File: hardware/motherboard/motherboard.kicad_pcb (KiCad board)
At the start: 4 copper layers, 152 x 68 mm, 79 parts, among them J1 IMU Connector, J2 JST-VH, J3 JST-VH, J4 JST-PH, J5 USB C 2.0, Q1 TSM7P06CP_ROG, Q2 TSM7P06CP_ROG, SW1 A, SW10 Right, SW11 Left, SW12 Up, SW2 B, SW3 X, SW4 Y, SW7 Start, SW8 Select, SW9 Down, U1 ESP32-S3-WROOM-1, U2 MCP73831-2-OT, U3 TPS75533KTTRG3, U4 TLV75709PDBV, U5 COM-09032

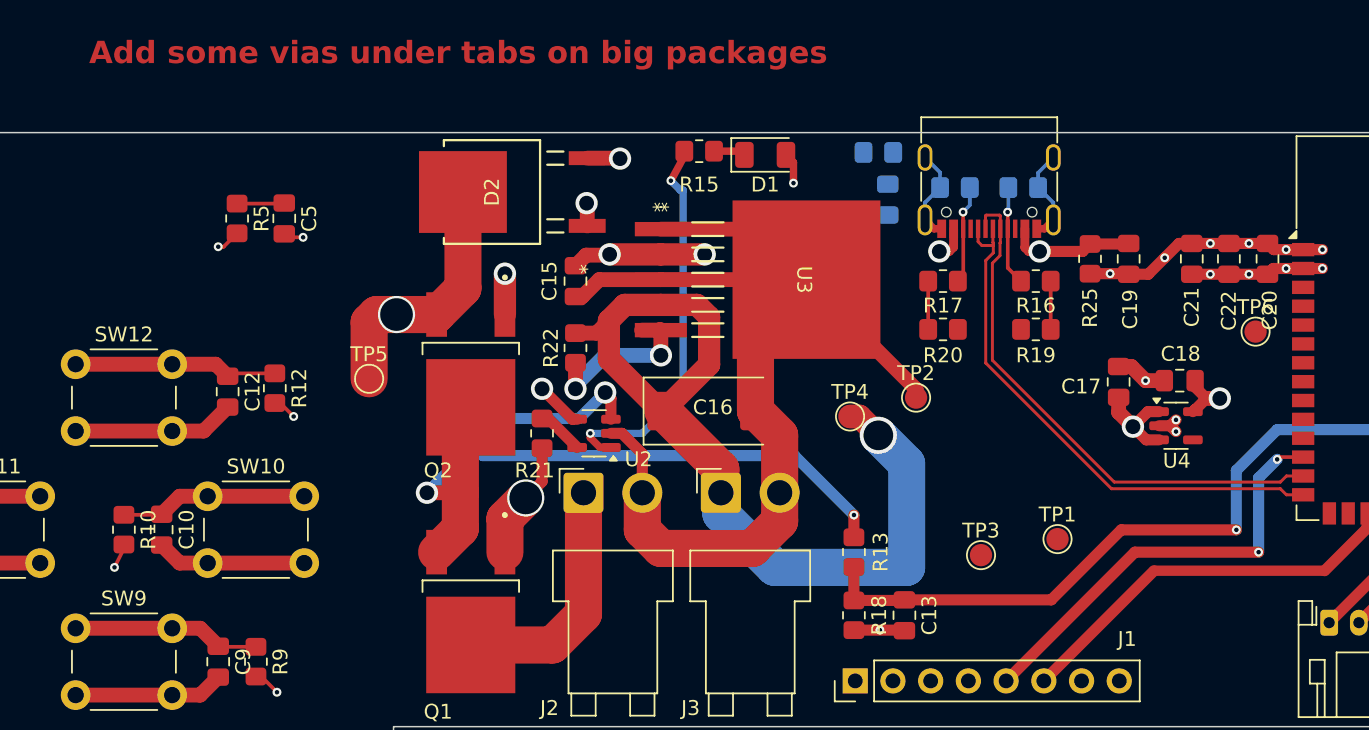
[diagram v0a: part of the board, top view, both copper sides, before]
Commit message: Moved Test Points
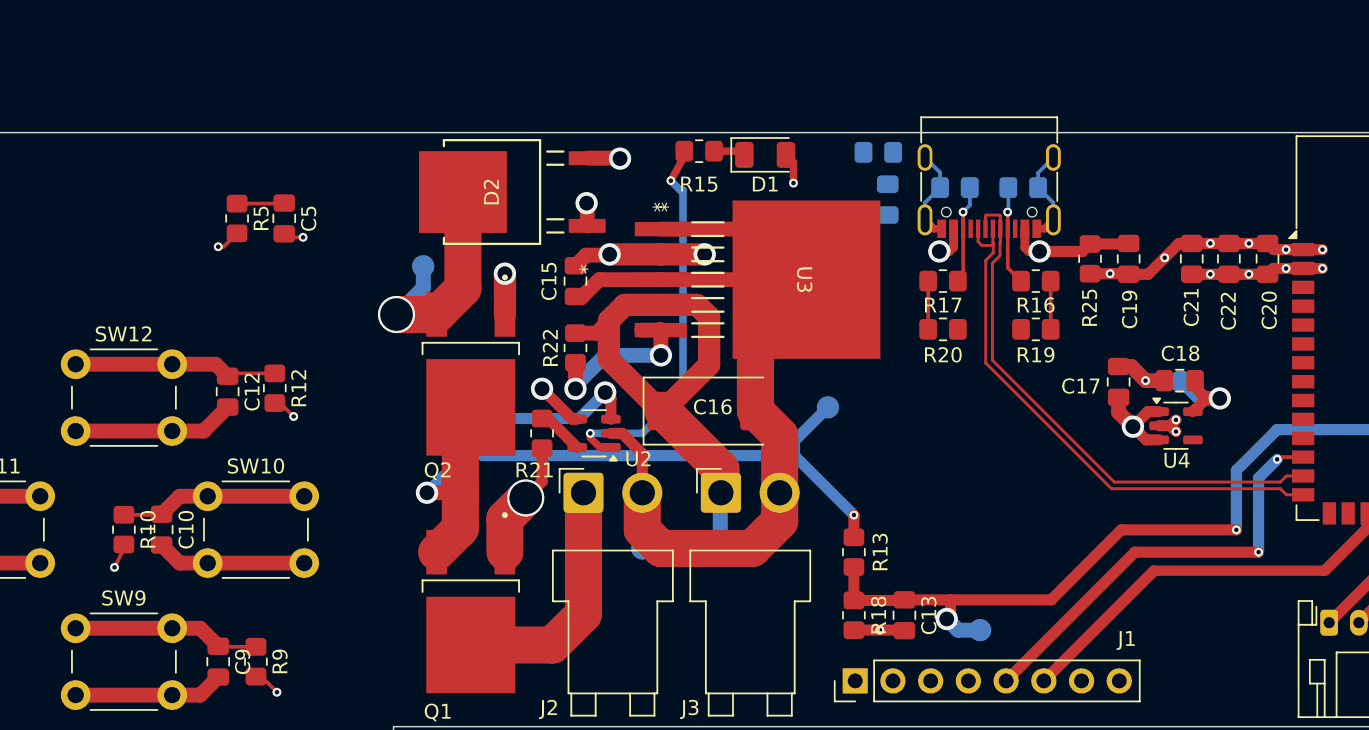
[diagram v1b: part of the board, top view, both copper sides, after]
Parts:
- TP1, TP2, TP3, TP4, TP5, TP6: moved to B.Cu
- moved TP2 21.0 mm to (64.8, 40.0), turned to 180 degrees
- moved TP3 14.3 mm to (77.2, 30.5), turned to 180 degrees
- moved TP4 12.5 mm to (70.0, 40.0), turned to 180 degrees
- moved TP5 8.41 mm to (50.0, 21.0), turned to 180 degrees
- moved TP1 8.04 mm to (87.5, 45.5), turned to 180 degrees
- moved TP6 6.06 mm to (101.0, 28.8), turned to 180 degrees
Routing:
- net VPeripheral: track 60.7 -> 36.3 mm, vias 1 -> 0
- net GND: track 234.5 -> 227.2 mm
- net VBat: track 73.5 -> 77.7 mm
- net ABat: track 65.4 -> 69.4 mm, vias 2 -> 3
- net +3V3: track 33.0 -> 36.1 mm
- net VIN: track 117.6 -> 115.7 mm
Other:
- board text removed: "Add some vias under tabs on big packages"

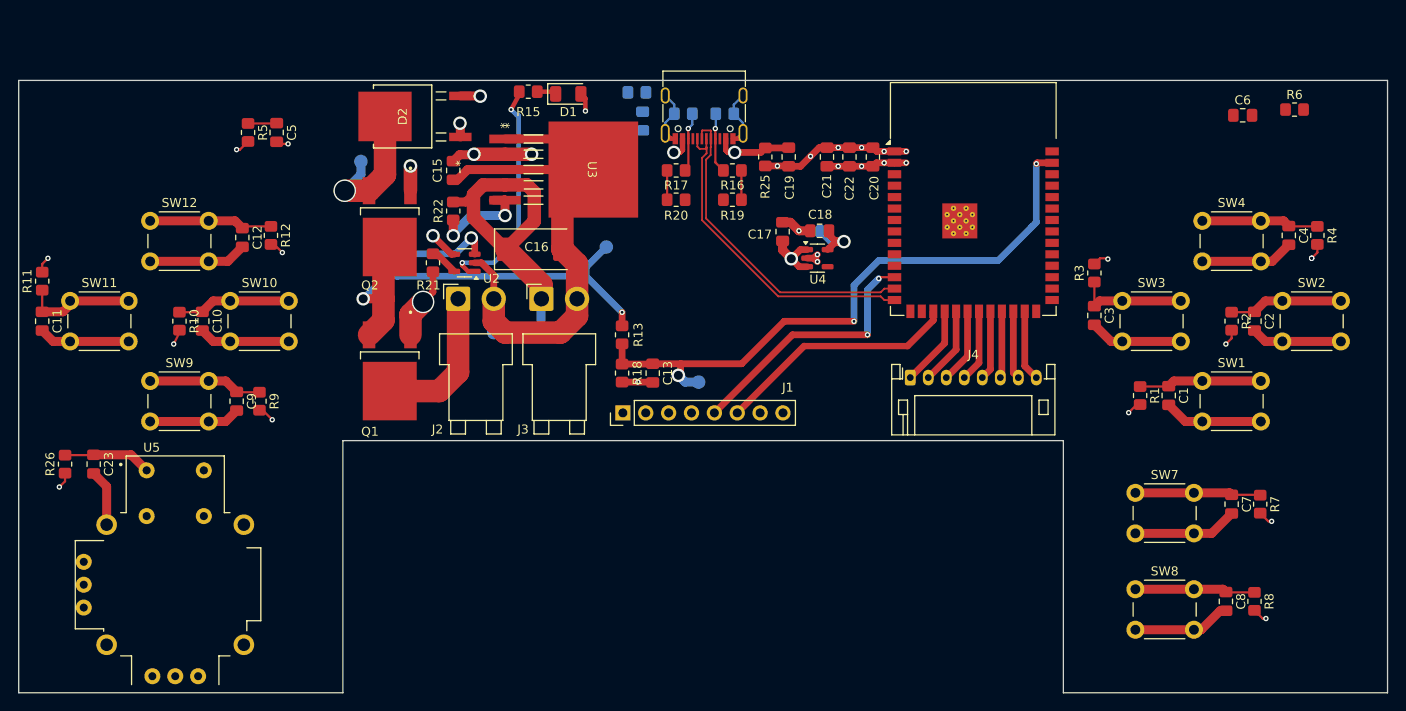
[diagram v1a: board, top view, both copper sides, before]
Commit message: Added bumper buttons
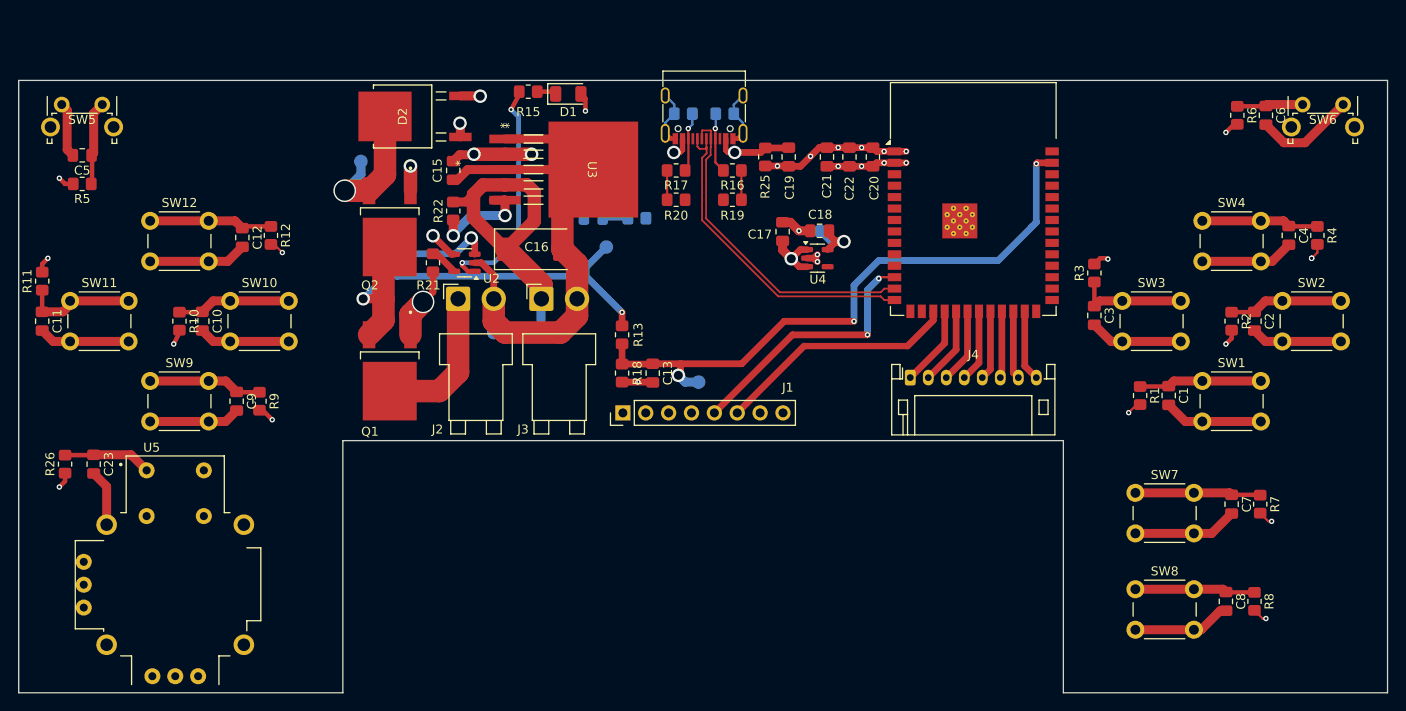
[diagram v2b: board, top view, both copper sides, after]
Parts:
- added SW5: LB, Button_Switch_THT:SW_Tactile_SPST_Angled_PTS645Vx58-2LFS, F.Cu at (16.8, 14.7)
- added SW6: RB, Button_Switch_THT:SW_Tactile_SPST_Angled_PTS645Vx58-2LFS, F.Cu at (154.6, 14.7)
- R21: value ??? -> 2k
- moved C5 21.7 mm to (19.1, 20.3), turned to 180 degrees
- moved R5 19.3 mm to (19.1, 23.5), turned to 180 degrees
- moved R14 14.0 mm to (80.6, 27.3), turned to 0 degrees
- moved C14 12.1 mm to (75.8, 27.3), turned to 180 degrees
- moved R6 6.38 mm to (147.3, 15.9), turned to -90 degrees
- moved C6 2.58 mm to (150.5, 15.9), turned to -90 degrees
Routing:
- net GND: track 227.2 -> 243.5 mm, vias 12 -> 11
- net BRight: track 0.00 -> 7.33 mm
- net BLeft: track 3.19 -> 9.37 mm
- net En: track 0.00 -> 2.81 mm
- net +3V3: track 36.1 -> 37.9 mm, vias 18 -> 19

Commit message: Adjusted Bumper Button Positions
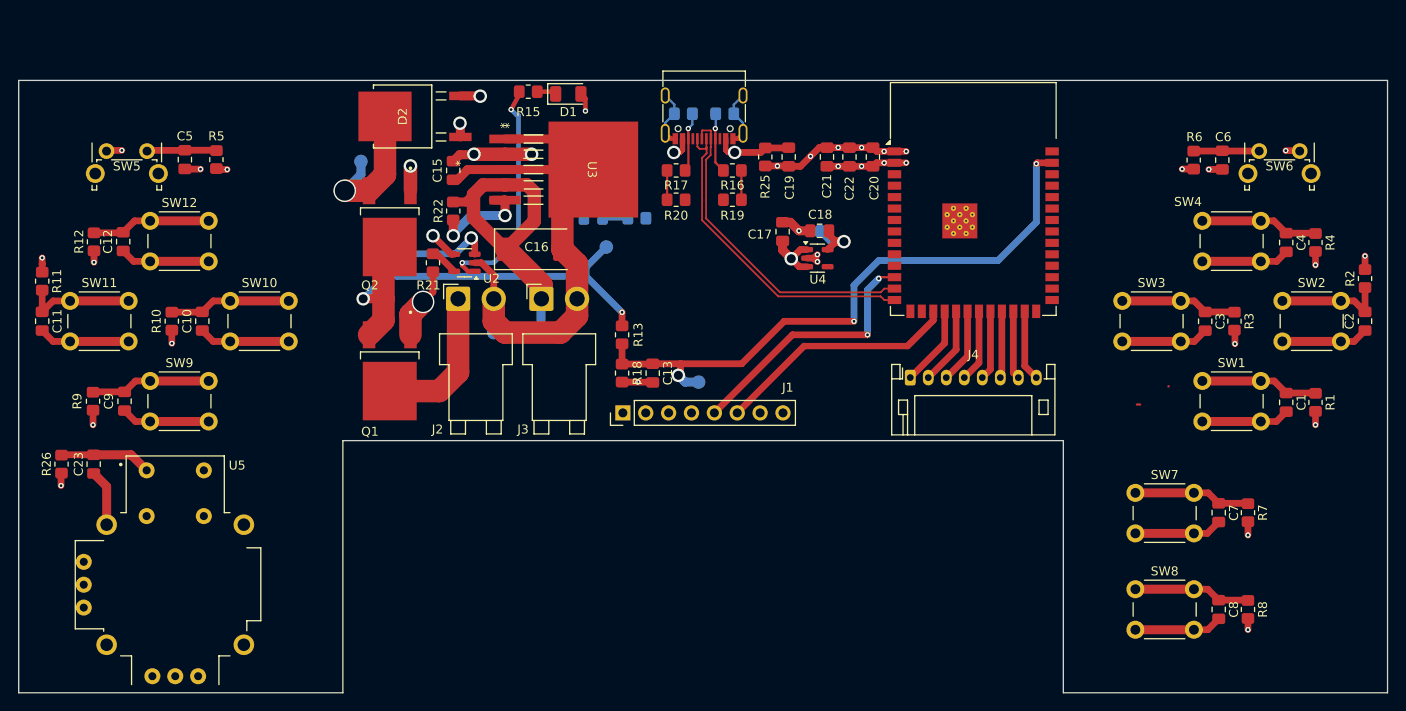
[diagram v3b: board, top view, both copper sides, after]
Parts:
- moved R12 19.7 mm to (20.4, 29.9)
- moved R1 19.5 mm to (156.0, 47.8)
- moved R9 18.5 mm to (20.2, 47.6)
- moved R3 16.4 mm to (147.0, 38.7), turned to -90 degrees
- moved R2 15.6 mm to (161.5, 34.0), turned to 90 degrees
- moved R5 15.1 mm to (34.0, 20.8), turned to -90 degrees
- moved C12 13.2 mm to (23.6, 29.9)
- moved C1 13.1 mm to (152.8, 47.8)
- moved C9 12.4 mm to (23.8, 47.6)
- moved C3 12.3 mm to (143.8, 38.8)
- moved C2 12.3 mm to (161.5, 38.7)
- moved C5 11.4 mm to (30.4, 20.8), turned to -90 degrees
- moved SW5 7.17 mm to (21.8, 19.9)
- moved SW6 7.07 mm to (149.8, 19.9)
- moved C6 6.94 mm to (145.7, 20.8)
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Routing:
- net GND: track 243.5 -> 224.8 mm, vias 11 -> 15
- net +3V3: track 37.9 -> 34.8 mm, vias 19 -> 18
- net BLeft: track 9.37 -> 7.76 mm
- net Start: track 14.0 -> 13.0 mm
- net Right: track 12.7 -> 13.5 mm
- net Down: track 12.7 -> 13.4 mm
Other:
- board text removed: "Left Bumper"
- board text removed: "Right Bumper"

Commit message: 12mm Corners
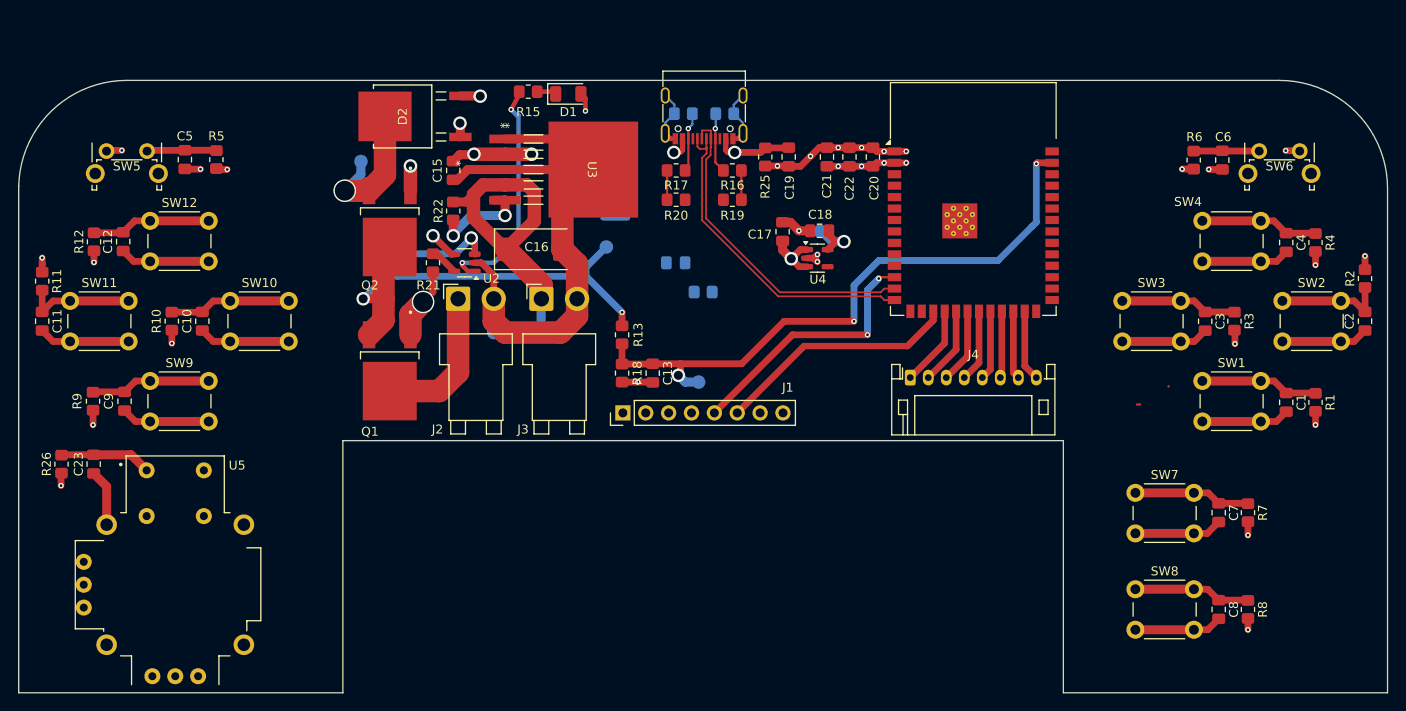
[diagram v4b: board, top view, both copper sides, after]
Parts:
- moved R14 11.0 mm to (88.0, 35.5)
- moved C14 10.4 mm to (85.0, 32.2)
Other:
- outline, holes or cut-outs redrawn
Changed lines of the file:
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@@
 	(footprint "Resistor_SMD:R_0805_2012Metric_Pad1.20x1.40mm_HandSolder"
 		(layer "B.Cu")
-		(at 80.645 27.305)
+		(at 88 35.5)
 		(descr "Resistor SMD 0805 (2012 Metric), square (rectangular) end terminal, IPC-7351 nominal with elongated pad for handsoldering. (Body size source: IPC-SM-782 page 72, https://www.pcb-3d.com/wordpress/wp-content/uploads/ipc-sm-782a_amendment_1_and_2.pdf), generated with kicad-footprint-generator")
 		(tags "resistor handsolder")
@@
 	(footprint "Capacitor_SMD:C_0805_2012Metric_Pad1.18x1.45mm_HandSolder"
 		(layer "B.Cu")
-		(at 75.7975 27.305 180)
+		(at 84.9625 32.25 180)
 		(descr "Capacitor SMD 0805 (2012 Metric), square (rectangular) end terminal, IPC-7351 nominal with elongated pad for handsoldering. (Body size source: IPC-SM-782 page 76, https://www.pcb-3d.com/wordpress/wp-content/uploads/ipc-sm-782a_amendment_1_and_2.pdf, https://docs.google.com/spreadsheets/d/1BsfQQcO9C6DZCsRaXUlFlo91Tg2WpOkGARC1WS5S8t0/edit?usp=sharing), generated with kicad-footprint-generator")
 		(tags "capacitor handsolder")
@@
 		(layer "Dwgs.User")
 	)
-	(gr_arc
-		(start 157.015 12.056181)
-		(mid 161.960377 14.104623)
-		(end 164.008819 19.05)
-		(stroke
-			(width 0.15)
-			(type default)
-		)
-		(layer "Dwgs.User")
-	)
 	(gr_rect
 		(start 50 80)
@@
 		(layer "Dwgs.User")
 	)
+	(gr_line
+		(start 160.485281 15.517323)
+		(end 152 24.002604)
+		(stroke
+			(width 0.15)
+			(type solid)
+		)
+		(layer "Dwgs.User")
+	)
 	(gr_rect
 		(start 88 80)
@@
 	)
 	(gr_rect
-		(start 12 12)
-		(end 164 102)
-		(stroke
-			(width 0.05)
+		(start 48 52)
+		(end 88 102)
+		(stroke
+			(width 0.2)
 			(type solid)
 		)
@@
 		(layer "Dwgs.User")
 	)
-	(gr_arc
-		(start 12.056181 19.058819)
-		(mid 14.104624 14.113443)
-		(end 19.05 12.065)
+	(gr_line
+		(start 24 24)
+		(end 15.514719 15.514719)
 		(stroke
 			(width 0.15)
-			(type default)
-		)
-		(layer "Dwgs.User")
-	)
-	(gr_rect
-		(start 48 52)
-		(end 88 102)
-		(stroke
-			(width 0.2)
 			(type solid)
 		)
+		(layer "Eco1.User")
+	)
+	(gr_circle
+		(center 152 24.002604)
+		(end 164 24.002604)
+		(stroke
+			(width 0.15)
+			(type solid)
+		)
 		(fill no)
-		(layer "Dwgs.User")
+		(layer "Eco1.User")
+	)
+	(gr_circle
+		(center 24 24)
+		(end 36 24)
+		(stroke
+			(width 0.15)
+			(type solid)
+		)
+		(fill no)
+		(layer "Eco1.User")
 	)
 	(gr_line
-		(start 164 12)
+		(start 164 24)
 		(end 164 80)
 		(stroke
@@
 	(gr_line
 		(start 12 80)
-		(end 12 12)
+		(end 12 23.75)
 		(stroke
 			(width 0.1)
@@
 		(layer "Edge.Cuts")
 	)
+	(gr_arc
+		(start 12 23.75)
+		(mid 15.601731 15.424945)
+		(end 24 11.997396)
+		(stroke
+			(width 0.1)
+			(type default)
+		)
+		(layer "Edge.Cuts")
+	)
+	(gr_arc
+		(start 152 12)
+		(mid 160.485281 15.514719)
+		(end 164 24)
+		(stroke
+			(width 0.1)
+			(type default)
+		)
+		(layer "Edge.Cuts")
+	)
 	(gr_line
 		(start 128 80)
@@
 	)
 	(gr_line
-		(start 12 12)
-		(end 164 12)
+		(start 24 11.997396)
+		(end 152 11.997396)
 		(stroke
 			(width 0.1)
-			(type default)
+			(type solid)
 		)
 		(layer "Edge.Cuts")
